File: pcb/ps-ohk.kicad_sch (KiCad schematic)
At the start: 17 parts

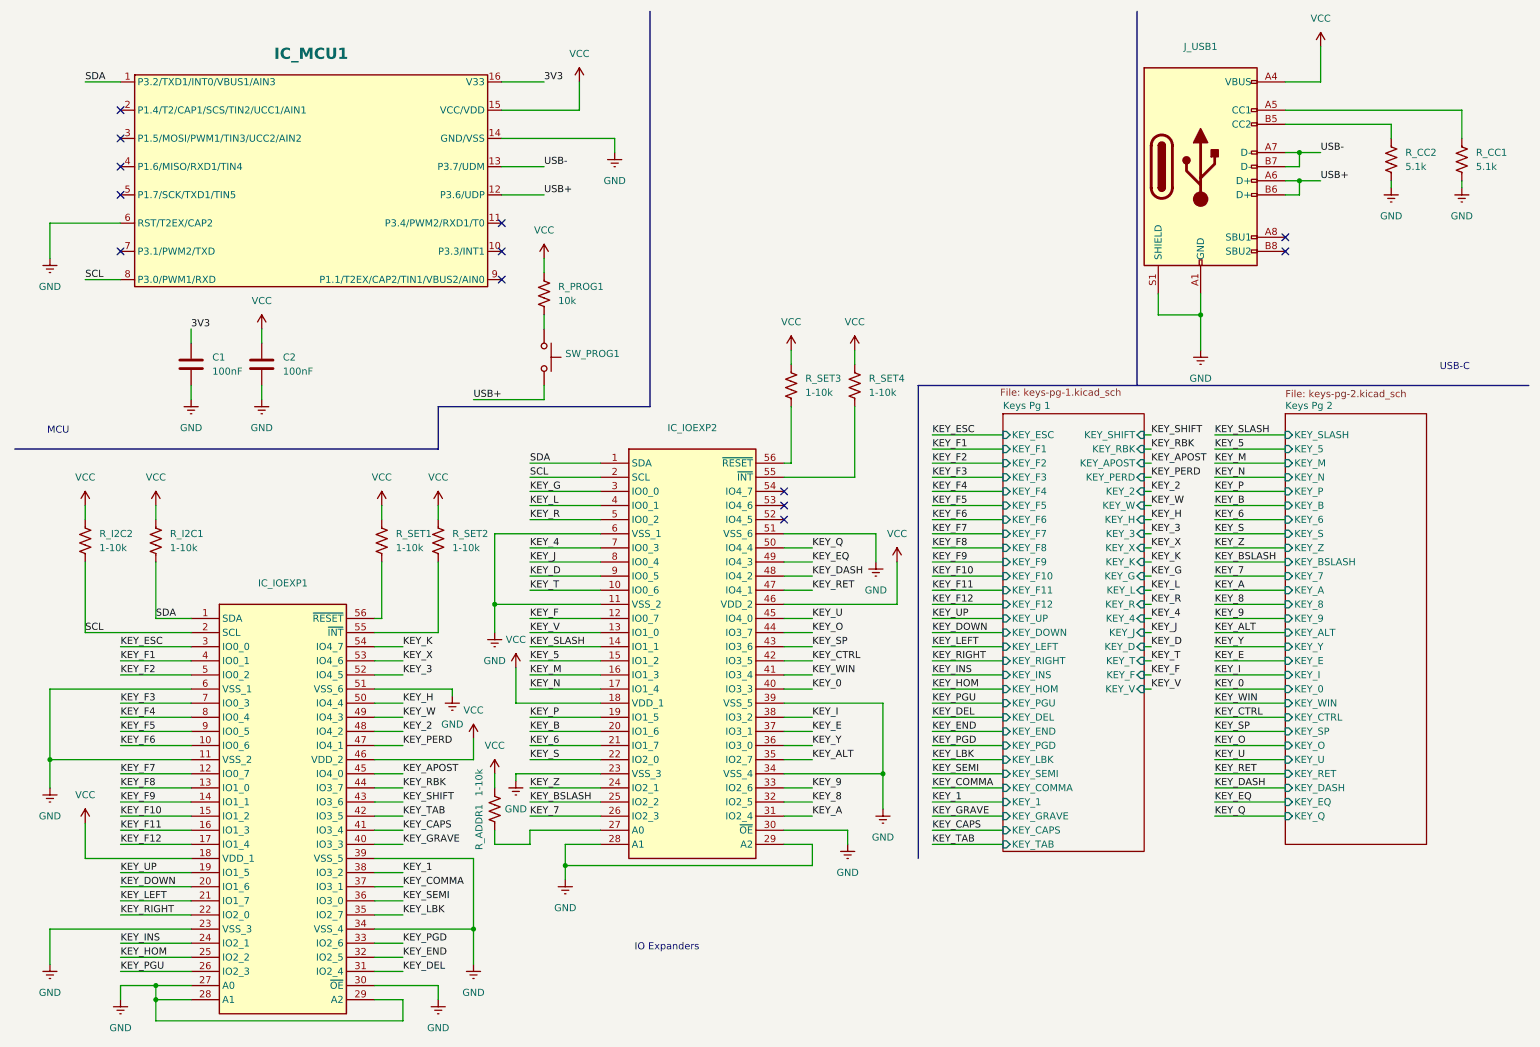
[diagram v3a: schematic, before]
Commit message: pcb: added C and rmd unneeded hardware
Signed-off-by: Dylan Turner <dylan.turner@tutanota.com>
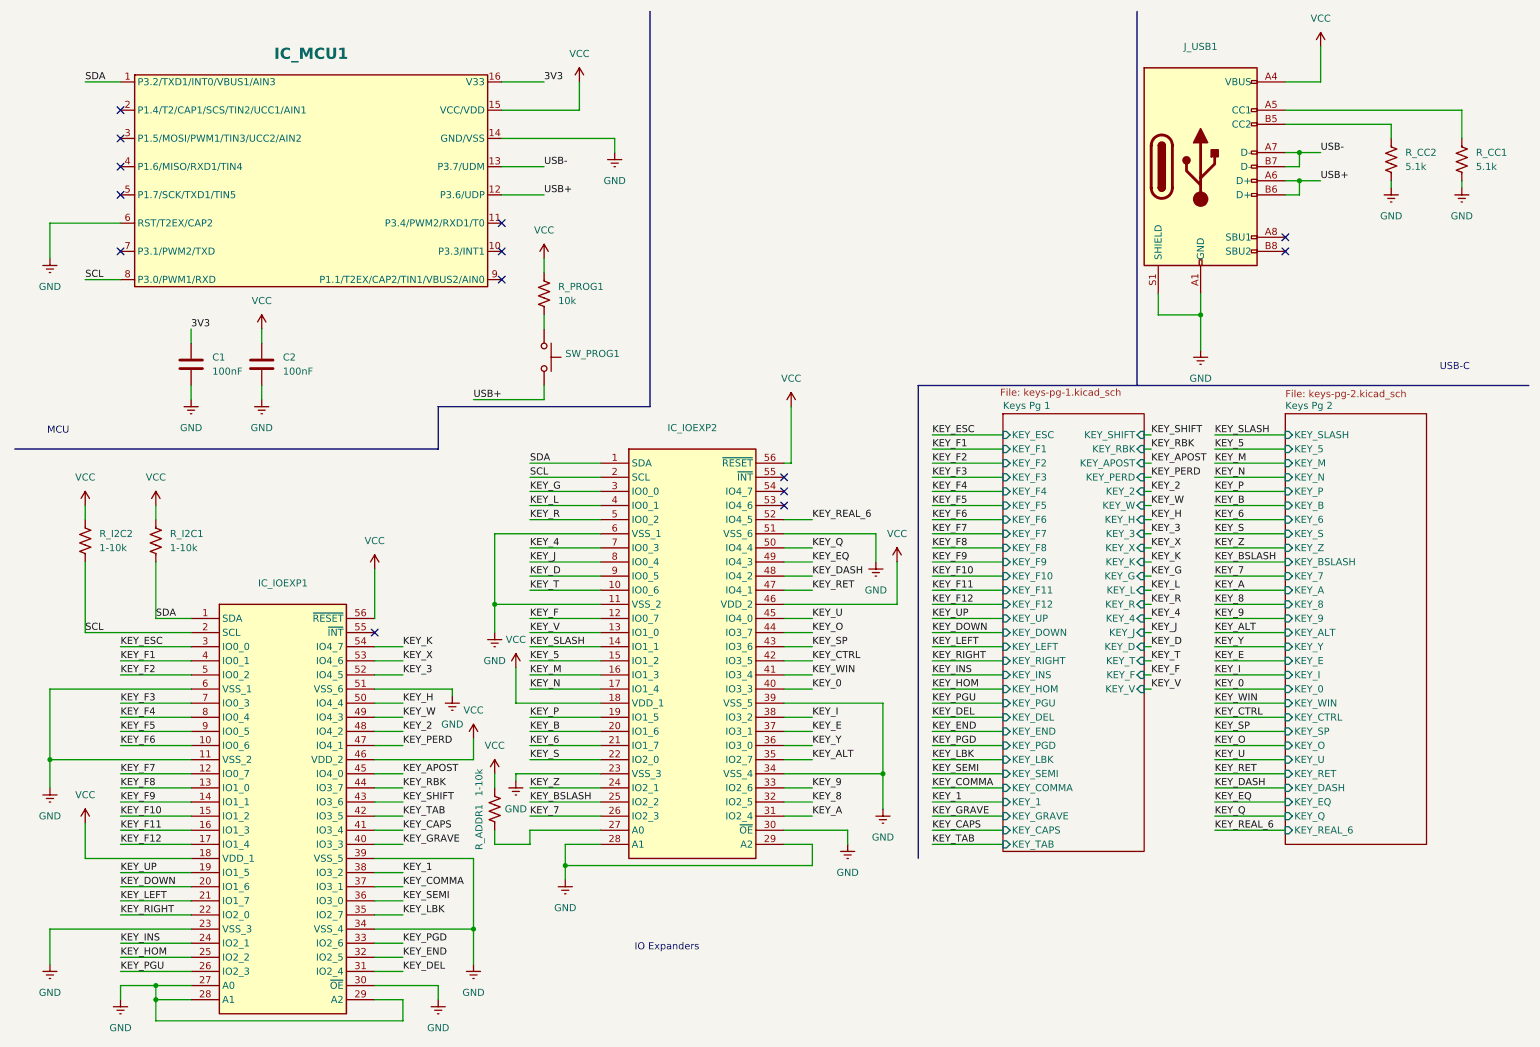
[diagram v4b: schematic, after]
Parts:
- removed R_SET1, R_SET2, R_SET3, R_SET4: 1-10k, Resistor_SMD:R_0603_1608Metric, symbol Device:R_US
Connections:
- net VCC: now also IC_IOEXP1.56 (~{RESET}), IC_IOEXP2.56 (~{RESET})
- net KEY_REAL_6: now reaches IC_IOEXP2.52 (IO4_5)
- no-connect marks 13 -> 14
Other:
- sheet Keys Pg 2 ports: added KEY_REAL_6; removed none

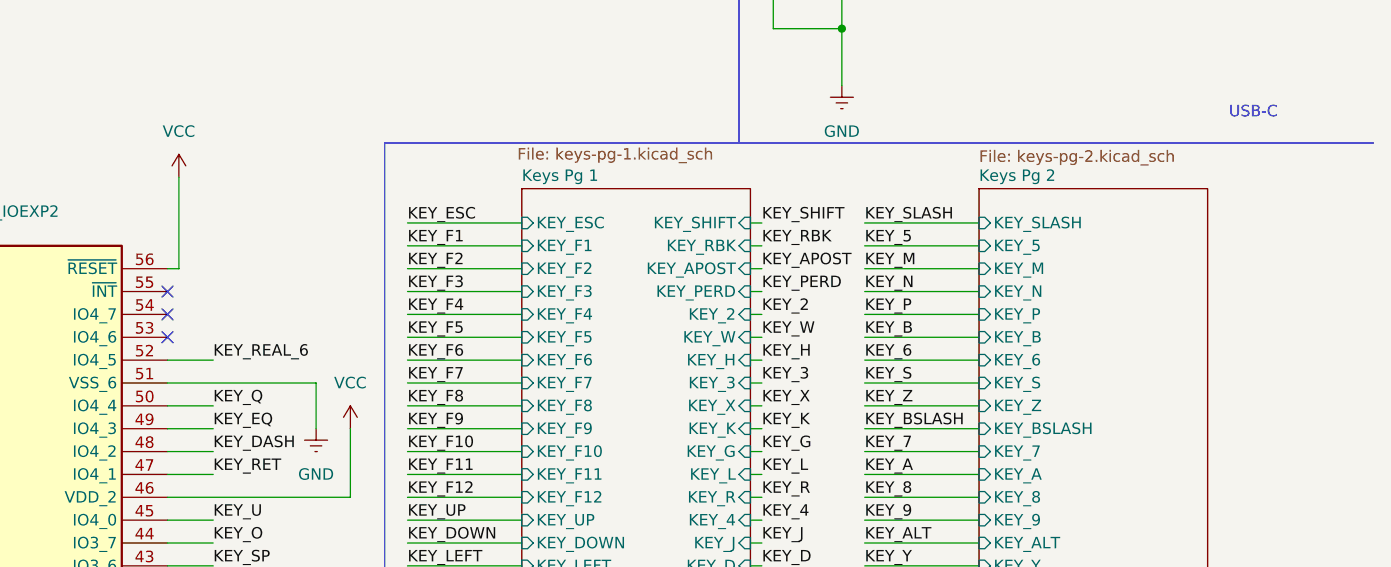
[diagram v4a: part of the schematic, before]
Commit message: pcb: add backspace and move k
Signed-off-by: Dylan Turner <dylan.turner@tutanota.com>
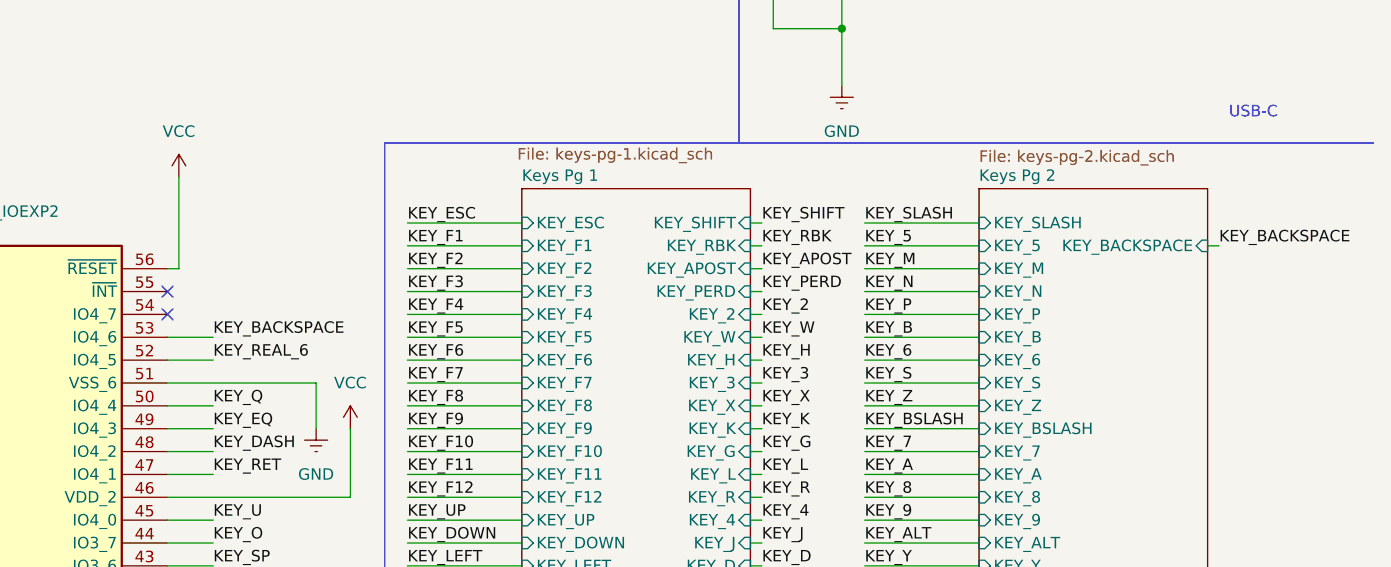
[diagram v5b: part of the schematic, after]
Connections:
- net KEY_BACKSPACE: now reaches IC_IOEXP2.53 (IO4_6)
- no-connect marks 14 -> 13
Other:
- sheet Keys Pg 2 ports: added KEY_BACKSPACE; removed none
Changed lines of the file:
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@@
 	)
 	(no_connect
-		(at 151.13 101.6)
-	)
-	(no_connect
 		(at 31.75 55.88)
 	)
@@
 	(wire
 		(pts
+			(xy 266.7 91.44) (xy 267.97 91.44)
+		)
+		(stroke
+			(width 0)
+			(type default)
+		)
+	)
+	(wire
+		(pts
 			(xy 177.8 142.24) (xy 190.5 142.24)
 		)
@@
 	(wire
 		(pts
+			(xy 156.21 101.6) (xy 151.13 101.6)
+		)
+		(stroke
+			(width 0)
+			(type default)
+		)
+	)
+	(wire
+		(pts
 			(xy 156.21 114.3) (xy 151.13 114.3)
 		)
@@
 		)
 	)
+	(label "KEY_BACKSPACE"
+		(at 267.97 91.44 0)
+		(fields_autoplaced yes)
+		(effects
+			(font
+				(size 1.27 1.27)
+			)
+			(justify left bottom)
+		)
+	)
 	(label "KEY_T"
 		(at 217.17 129.54 0)
@@
 		)
 	)
+	(label "KEY_BACKSPACE"
+		(at 156.21 101.6 0)
+		(fields_autoplaced yes)
+		(effects
+			(font
+				(size 1.27 1.27)
+			)
+			(justify left bottom)
+		)
+	)
 	(label "KEY_X"
 		(at 217.17 109.22 0)
@@
 			)
 		)
+		(pin "KEY_BACKSPACE" input
+			(at 266.7 91.44 0)
+			(effects
+				(font
+					(size 1.27 1.27)
+				)
+				(justify right)
+			)
+		)
